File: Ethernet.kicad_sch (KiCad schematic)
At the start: 23 parts, among them IC6 LAN8651B1-E_LMX, J7 RJ45_LED, Y4 Crystal_GND24

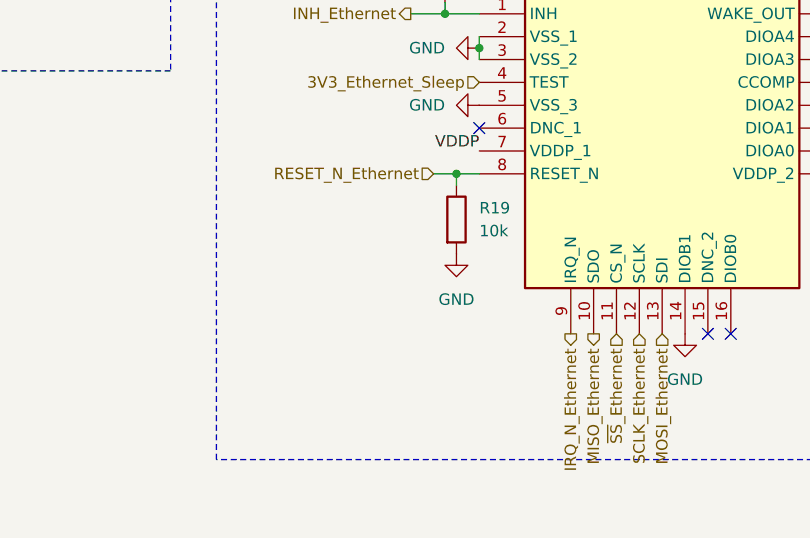
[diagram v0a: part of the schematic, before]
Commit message: Reorganise synoptic schematic for better reading Closes #26
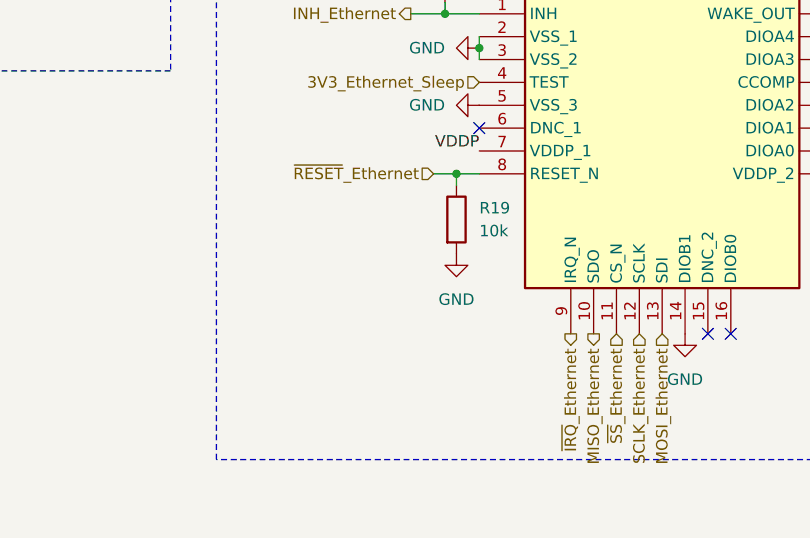
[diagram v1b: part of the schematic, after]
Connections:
- net IRQ_N_Ethernet renamed ~{IRQ}_Ethernet
- net RESET_N_Ethernet renamed ~{RESET}_Ethernet
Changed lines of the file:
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@@
 		)
 	)
-	(hierarchical_label "RESET_N_Ethernet"
+	(hierarchical_label "~{RESET}_Ethernet"
 		(shape input)
 		(at 128.27 116.84 180)
@@
 		)
 	)
-	(hierarchical_label "IRQ_N_Ethernet"
+	(hierarchical_label "~{IRQ}_Ethernet"
 		(shape output)
 		(at 143.51 134.62 270)

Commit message: Continue schematic review
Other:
- moved on the sheet: C74, R19
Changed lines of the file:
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@@
 	(text "LAN8651 25MHz oscillator"
 		(exclude_from_sim no)
-		(at 239.522 88.646 0)
+		(at 240.03 88.9 0)
 		(effects
 			(font
@@
 	(text "RJ45 Connector for LAN8651"
 		(exclude_from_sim no)
-		(at 240.284 45.466 0)
+		(at 240.03 45.72 0)
 		(effects
 			(font
@@
 	(text "External Ethernet PHY"
 		(exclude_from_sim no)
-		(at 112.268 56.896 0)
+		(at 111.76 45.72 0)
 		(effects
 			(font
@@
 	(text "Ethernet LAN8651 decoupling capacitors"
 		(exclude_from_sim no)
-		(at 37.592 45.466 0)
+		(at 38.1 45.72 0)
 		(effects
 			(font
@@
 	(text "Ethernet PHY"
 		(exclude_from_sim no)
-		(at 145.288 23.114 0)
+		(at 144.78 22.86 0)
 		(effects
 			(font
@@
 			(justify left top)
 		)
+	)
+	(junction
+		(at 129.54 116.84)
+		(diameter 0)
+		(color 0 0 0 0)
 	)
 	(junction
@@
 	)
 	(junction
-		(at 130.81 116.84)
-		(diameter 0)
-		(color 0 0 0 0)
-	)
-	(junction
 		(at 46.99 50.8)
 		(diameter 0)
@@
 	(wire
 		(pts
-			(xy 173.99 106.68) (xy 190.5 106.68)
+			(xy 173.99 106.68) (xy 187.96 106.68)
 		)
 		(stroke
@@
 	(wire
 		(pts
-			(xy 128.27 116.84) (xy 130.81 116.84)
+			(xy 125.73 116.84) (xy 129.54 116.84)
 		)
 		(stroke
@@
 	(wire
 		(pts
-			(xy 130.81 116.84) (xy 130.81 118.11)
+			(xy 129.54 116.84) (xy 129.54 118.11)
 		)
 		(stroke
@@
 	(wire
 		(pts
-			(xy 130.81 116.84) (xy 133.35 116.84)
-		)
-		(stroke
-			(width 0)
-			(type default)
-		)
-	)
-	(wire
-		(pts
 			(xy 125.73 99.06) (xy 129.54 99.06)
+		)
+		(stroke
+			(width 0)
+			(type default)
+		)
+	)
+	(wire
+		(pts
+			(xy 129.54 116.84) (xy 133.35 116.84)
 		)
 		(stroke
@@
 	(hierarchical_label "~{RESET}_Ethernet"
 		(shape input)
-		(at 128.27 116.84 180)
+		(at 125.73 116.84 180)
 		(effects
 			(font
@@
 	(symbol
 		(lib_id "Device:C")
-		(at 190.5 110.49 0)
+		(at 187.96 110.49 0)
 		(unit 1)
 		(exclude_from_sim no)
@@
 		(fields_autoplaced yes)
 		(property "Reference" "C74"
-			(at 194.31 109.2199 0)
+			(at 191.77 109.2199 0)
 			(effects
 				(font
@@
 		)
 		(property "Value" "4u7"
-			(at 194.31 111.7599 0)
+			(at 191.77 111.7599 0)
 			(effects
 				(font
@@
 		)
 		(property "Footprint" ""
-			(at 191.4652 114.3 0)
+			(at 188.9252 114.3 0)
 			(effects
 				(font
@@
 		)
 		(property "Datasheet" "~"
-			(at 190.5 110.49 0)
+			(at 187.96 110.49 0)
 			(effects
 				(font
@@
 		)
 		(property "Description" "Unpolarized capacitor"
-			(at 190.5 110.49 0)
+			(at 187.96 110.49 0)
 			(effects
 				(font
@@
 	(symbol
 		(lib_id "Device:R")
-		(at 130.81 121.92 0)
+		(at 129.54 121.92 0)
 		(unit 1)
 		(exclude_from_sim no)
@@
 		(fields_autoplaced yes)
 		(property "Reference" "R19"
-			(at 133.35 120.6499 0)
+			(at 132.08 120.6499 0)
 			(effects
 				(font
@@
 		)
 		(property "Value" "10k"
-			(at 133.35 123.1899 0)
+			(at 132.08 123.1899 0)
 			(effects
 				(font
@@
 		)
 		(property "Footprint" ""
-			(at 129.032 121.92 90)
+			(at 127.762 121.92 90)
 			(effects
 				(font
@@
 		)
 		(property "Datasheet" "~"
-			(at 130.81 121.92 0)
+			(at 129.54 121.92 0)
 			(effects
 				(font
@@
 		)
 		(property "Description" "Resistor"
-			(at 130.81 121.92 0)
+			(at 129.54 121.92 0)
 			(effects
 				(font
@@
 	(symbol
 		(lib_id "power:GND")
-		(at 130.81 125.73 0)
+		(at 129.54 125.73 0)
 		(unit 1)
 		(exclude_from_sim no)
@@
 		(fields_autoplaced yes)
 		(property "Reference" "#PWR0127"
-			(at 130.81 132.08 0)
+			(at 129.54 132.08 0)
 			(effects
 				(font
@@
 		)
 		(property "Value" "GND"
-			(at 130.81 130.81 0)
+			(at 129.54 130.81 0)
 			(effects
 				(font
@@
 		)
 		(property "Footprint" ""
-			(at 130.81 125.73 0)
+			(at 129.54 125.73 0)
 			(effects
 				(font
@@
 		)
 		(property "Datasheet" ""
-			(at 130.81 125.73 0)
+			(at 129.54 125.73 0)
 			(effects
 				(font
@@
 		)
 		(property "Description" "Power symbol creates a global label with name \"GND\" , ground"
-			(at 130.81 125.73 0)
+			(at 129.54 125.73 0)
 			(effects
 				(font
@@
 	(symbol
 		(lib_id "power:GND")
-		(at 190.5 114.3 0)
+		(at 187.96 114.3 0)
 		(unit 1)
 		(exclude_from_sim no)
@@
 		(fields_autoplaced yes)
 		(property "Reference" "#PWR0117"
-			(at 190.5 120.65 0)
+			(at 187.96 120.65 0)
 			(effects
 				(font
@@
 		)
 		(property "Value" "GND"
-			(at 190.5 119.38 0)
+			(at 187.96 119.38 0)
 			(effects
 				(font
@@
 		)
 		(property "Footprint" ""
-			(at 190.5 114.3 0)
+			(at 187.96 114.3 0)
 			(effects
 				(font
@@
 		)
 		(property "Datasheet" ""
-			(at 190.5 114.3 0)
+			(at 187.96 114.3 0)
 			(effects
 				(font
@@
 		)
 		(property "Description" "Power symbol creates a global label with name \"GND\" , ground"
-			(at 190.5 114.3 0)
-			(effects
-				(font
+			(at 187.96 114.3 0)
+			(effects
+				(font

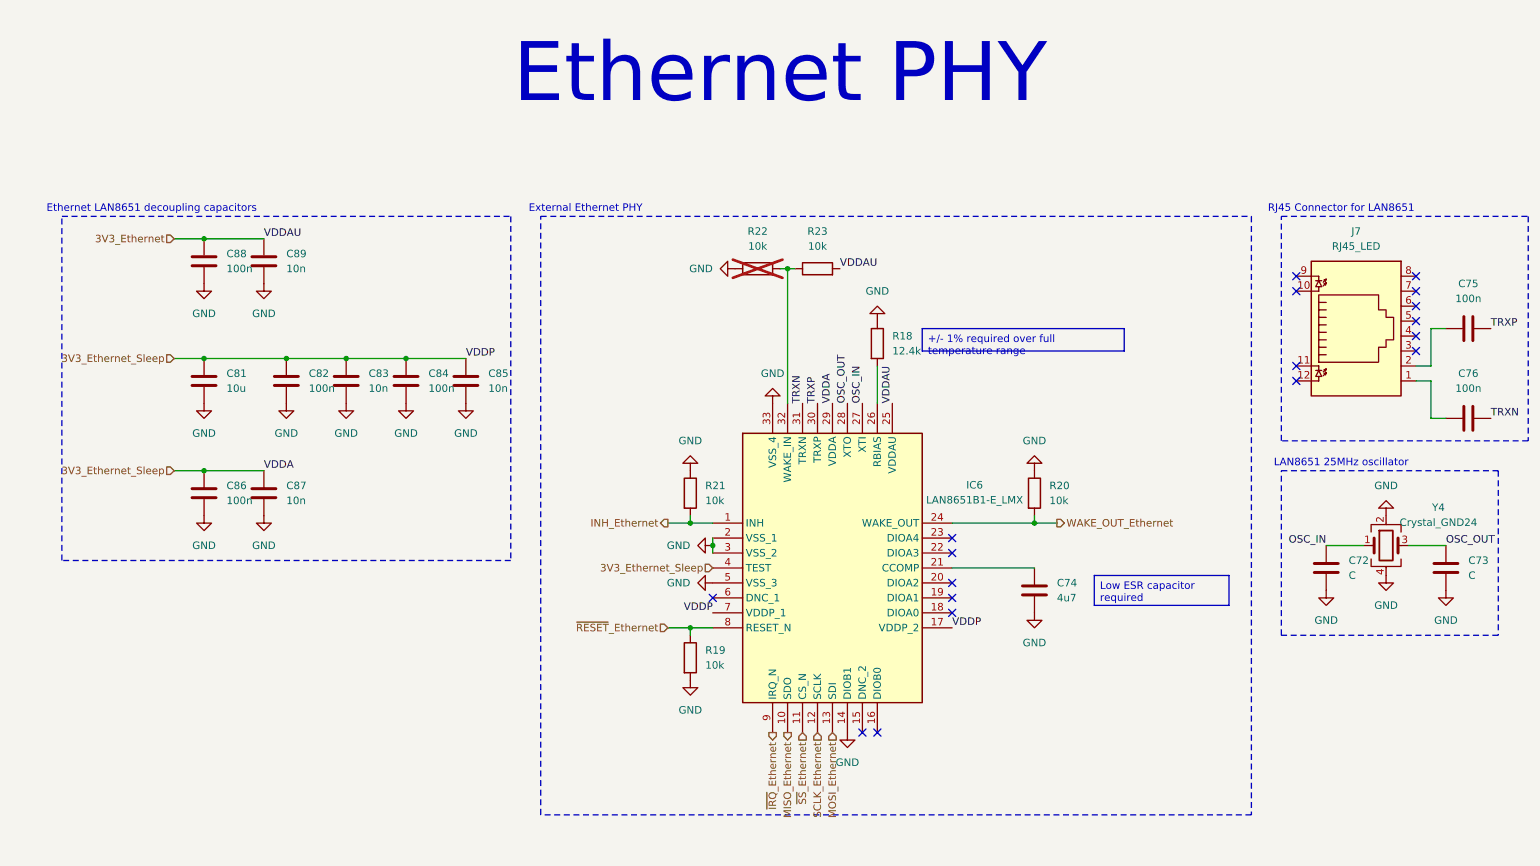
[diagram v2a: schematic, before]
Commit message: Fix some little warnings and refomat schematics files
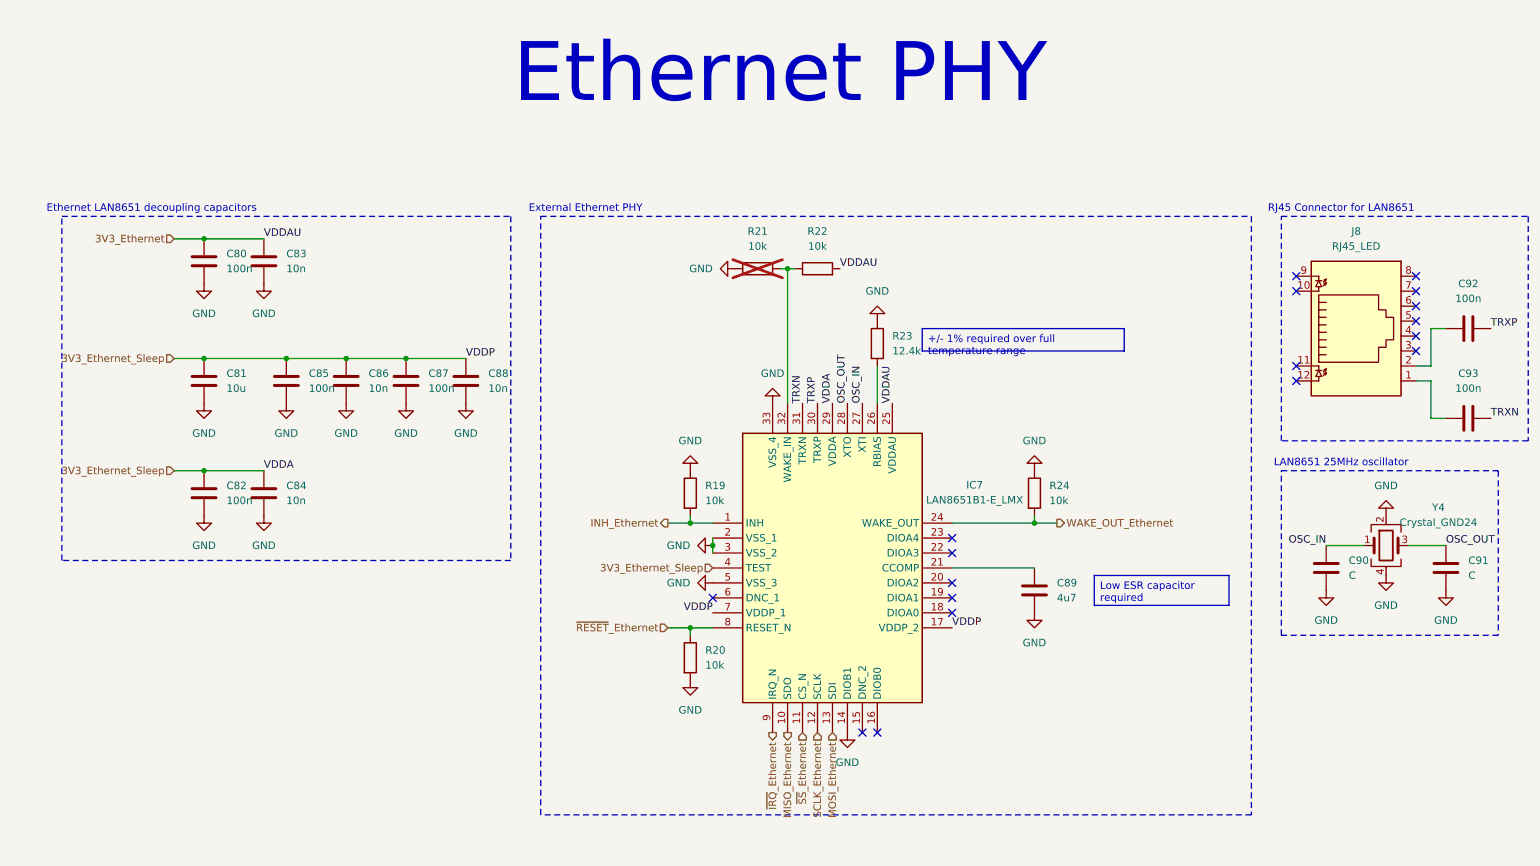
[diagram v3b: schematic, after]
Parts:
- renumbered C88 to C80, C86 to C82, C89 to C83, C87 to C84, C82 to C85, C83 to C86, C84 to C87, C85 to C88, C74 to C89, C72 to C90, C73 to C91, C75 to C92, C76 to C93, IC6 to IC7, J7 to J8, R21 to R19, R19 to R20, R22 to R21, R23 to R22, R18 to R23, R20 to R24
